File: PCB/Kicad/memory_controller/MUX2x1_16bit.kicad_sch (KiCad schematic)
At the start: 8 parts, among them U3 74LS245, U4 74LS245, U5 74LS245, U6 74LS245

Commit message: fix
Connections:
- net nOE_n renamed ~{OE}_n
- net nOE_p renamed ~{OE}_p
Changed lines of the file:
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@@
-		)
-	)
-	(hierarchical_label "nOE_n"
-		(shape input)
-		(at 90.17 148.59 180)
-		(effects
-			(font
-				(size 1.016 1.016)
-			)
-			(justify right)
 		)
 	)
@@
 		)
 	)
-	(hierarchical_label "nOE_n"
+	(hierarchical_label "~{OE}_n"
 		(shape input)
 		(at 88.9 93.98 180)
@@
 		)
 	)
-	(hierarchical_label "nOE_p"
+	(hierarchical_label "~{OE}_n"
 		(shape input)
-		(at 151.13 93.98 180)
+		(at 90.17 148.59 180)
 		(effects
 			(font
@@
 		)
 	)
-	(hierarchical_label "nOE_p"
+	(hierarchical_label "~{OE}_p"
 		(shape input)
-		(at 151.13 148.59 180)
+		(at 151.13 93.98 180)
 		(effects
 			(font
@@
 		)
 	)
+	(hierarchical_label "~{OE}_p"
+		(shape input)
+		(at 151.13 148.59 180)
+		(effects
+			(font
+				(size 1.016 1.016)
+			)
+			(justify right)
+		)
+	)

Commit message: pcb init
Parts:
- C3, C4, C5, C6: footprint (none) -> Capacitor_SMD:C_0402_1005Metric
- U3, U4, U5, U6: footprint (none) -> Package_SO:SOIC-20W_7.5x12.8mm_P1.27mm
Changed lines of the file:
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@@
 			)
 		)
-		(property "Footprint" ""
+		(property "Footprint" "Package_SO:SOIC-20W_7.5x12.8mm_P1.27mm"
 			(at 165.1 135.89 0)
 			(effects
@@
 			)
 		)
-		(property "Footprint" ""
+		(property "Footprint" "Package_SO:SOIC-20W_7.5x12.8mm_P1.27mm"
 			(at 165.1 81.28 0)
 			(effects
@@
 			)
 		)
-		(property "Footprint" ""
+		(property "Footprint" "Capacitor_SMD:C_0402_1005Metric"
 			(at 179.3748 96.52 0)
 			(effects
@@
 			)
 		)
-		(property "Footprint" ""
+		(property "Footprint" "Package_SO:SOIC-20W_7.5x12.8mm_P1.27mm"
 			(at 106.68 135.89 0)
 			(effects
@@
 			)
 		)
-		(property "Footprint" ""
+		(property "Footprint" "Capacitor_SMD:C_0402_1005Metric"
 			(at 185.7248 148.59 0)
 			(effects
@@
 			)
 		)
-		(property "Footprint" ""
+		(property "Footprint" "Capacitor_SMD:C_0402_1005Metric"
 			(at 87.9348 166.37 0)
 			(effects
@@
 			)
 		)
-		(property "Footprint" ""
+		(property "Footprint" "Package_SO:SOIC-20W_7.5x12.8mm_P1.27mm"
 			(at 106.68 81.28 0)
 			(effects
@@
 			)
 		)
-		(property "Footprint" ""
+		(property "Footprint" "Capacitor_SMD:C_0402_1005Metric"
 			(at 120.9548 96.52 0)
 			(effects

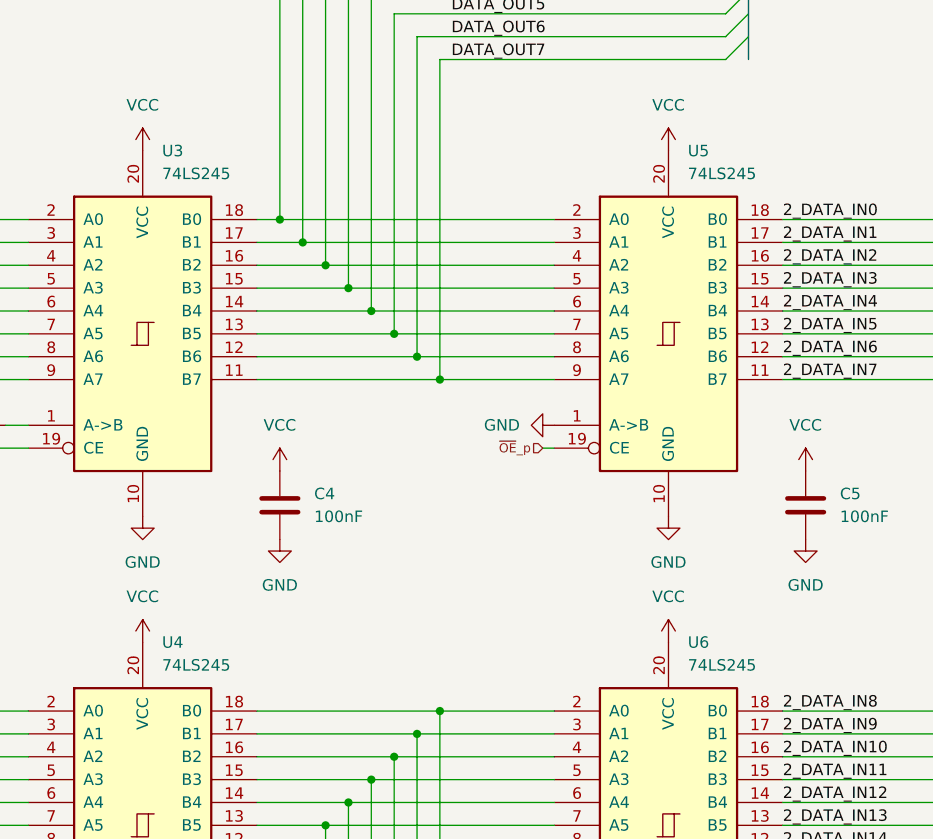
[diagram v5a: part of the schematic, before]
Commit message: memory controller schematic update
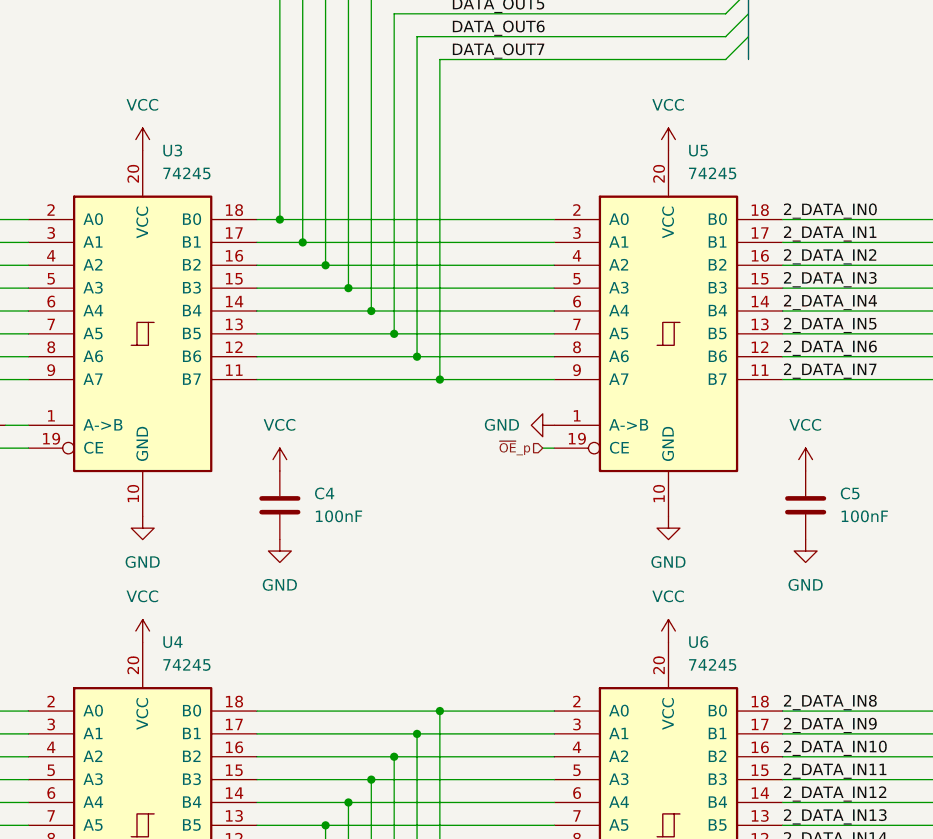
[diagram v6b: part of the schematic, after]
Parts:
- U3, U4, U5, U6: value 74LS245 -> 74245; footprint Package_SO:SOIC-20W_7.5x12.8mm_P1.27mm -> Package_SO:TSSOP-20_4.4x6.5mm_P0.65mm
